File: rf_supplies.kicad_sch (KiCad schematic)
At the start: 27 parts, among them J20 VSENSE, U14 INA290A2xDCK

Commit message: wip
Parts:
- removed R100, R102, R104, R106: 453k, Resistor_SMD:R_0402_1005Metric, symbol Device:R_Small
- removed R101, R103, R105, R107: 33k, Resistor_SMD:R_0402_1005Metric, symbol Device:R_Small
- R109: value 60k -> 70k
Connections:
- no-connect marks 6 -> 2
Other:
- sheet Switching TX 6V renamed RF Switching 7V
- removed sheet Linear POL LMK DIG
- removed sheet Linear POL LMK VCO
- removed sheet Linear POL LMX
- removed sheet Linear POL LMX BUF
- removed sheet OP Amp Supply
- moved on the sheet: R108, R109

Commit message: Add Clock sources and monitor output
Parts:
- renumbered C102 to C106, C103 to C107, C104 to C108, C105 to C109, D11 to D10, J20 to J26, L6 to L5, R93 to R86, R94 to R87, R95 to R88, R96 to R89, R97 to R90, R98 to R91, R99 to R92, R108 to R93, R109 to R94, U14 to U20

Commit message: It's finished (well the draft)
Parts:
- added R?: 49.9k, Resistor_SMD:R_0402_1005Metric, symbol Device:R_Small
- added R?: 267k, Resistor_SMD:R_0402_1005Metric, symbol Device:R_Small
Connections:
- net +7V: now also R?.1
- net GND: now also R?.2
- net RF_ISENSE renamed RF12_ISENSE
- net RF_SENSE renamed RF12_SENSE
- new net RF7_SENSE: R?.1, R?.2
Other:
- moved on the sheet: R87, R88, R89, R90, R91, R92

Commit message: Round 1 review comments
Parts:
- added R?: 1.8k, Resistor_THT:R_Array_SIP4, symbol Device:R_Small
- added R?: 4.7k, Resistor_THT:R_Array_SIP4, symbol Device:R_Small
- R146: renamed from R93; value 357k -> 619k
- R147: renamed from R94; value 70k -> 49.9k
- gave numbers to parts that had none: 2
- renumbered C106 to C140, C107 to C141, C108 to C142, C109 to C143, J26 to J29, R86 to R137, R87 to R138, R88 to R139, R89 to R140, R90 to R141, R91 to R144, R92 to R145, U20 to U21
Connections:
- net +7V: now also R?.1
- net GND: now also R?.2
- new net RF Switching 7V/OUTS: R?.1, R?.2
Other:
- sheet RF Switching 7V ports: added OUTS; removed none
- sheet RF Switching PSU ports: added OUTS; removed none

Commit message: Round 2 Review, power tree cleanup
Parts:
- added FB?: 74279228600, Inductor_SMD:L_0603_1608Metric, symbol Device:FerriteBead_Small
- R156: renamed from R146; now not fitted
- R157: renamed from R147; now not fitted
- R158, R159: renamed from R?; now not fitted
- renumbered C140 to C142, C141 to C143, C142 to C144, C143 to C145, J29 to J30, R137 to R147, R138 to R148, R139 to R149, R140 to R150, R141 to R151, R142 to R152, R143 to R153, R144 to R154, R145 to R155
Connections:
- net +12V_RF: now also FB?.1
- net +7V: now also FB?.2
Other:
- note added: "1.1RPI"
- note added: "12VRF"
- note added: "3.3LMKDIG"
- note added: "3.3LMKVCO"
- note added: "3.3LMX"
- note added: "3.3LMXBUF"
- note added: "3.3MCU"
- note added: "3.3VAMP1"
- note added: "3.3VAMP2"
- note added: "3.3VLNA"
- note added: "3.3VRXDIG"
- note added: "3.3VTXDIG"
- note added: "4V"
- note added: "4VRX"
- note added: "5A FUSE + FILTER 250mV/A ISENSE"
- note added: "5V"
- note added: "7VLO"
- note added: "LMR36510ADDA 12V->5.0V1A"
- note added: "LT3042 4V->3.3V0.2A"
- note added: "LT3045 4V->3.3V0.5A"
- note added: "LT3045 7V/12V->5V0.5A"
- note added: "LT8625S uMOD 12V->4V8A"
- note added: "LT8625S uMOD 12V->7V8A"
- note added: "Regulator is for if we run into thermal issues"
- note added: "TLV73311PDBV 3.3V->1.1V0.3A"
- note added: "TLV73333PDBV 4V->3.3V0.3A"
- note added: "TLV73333PDBV 5V->3.3V0.3A"
- note added: "VBUS"
- note added: "VDC"
- note added: "x2"
- moved on the sheet: C142, C143, C144, C145, D10, F1, FB1, J30, L5, R147, R148, R149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

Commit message: Darrel Suggestions
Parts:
- R158, R159: footprint Resistor_THT:R_Array_SIP4 -> (none)
- gave numbers to parts that had none: 1
- renumbered FB1 to FB3, L5 to L3
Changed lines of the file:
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@@
 		(dnp no)
 		(fields_autoplaced yes)
-		(property "Reference" "#PWR0171"
+		(property "Reference" "#PWR0173"
 			(at 71.12 27.94 0)
 			(hide yes)
@@
 			(project "huskypointofload"
 				(path "/eb9c972b-d134-41da-be97-ece3f463f7e0/28dccbc8-62a2-4750-b12f-4e220cef19bd"
-					(reference "#PWR0171")
+					(reference "#PWR0173")
 					(unit 1)
 				)
@@
 		(dnp no)
 		(fields_autoplaced yes)
-		(property "Reference" "#PWR0189"
+		(property "Reference" "#PWR0193"
 			(at 394.97 36.83 0)
 			(hide yes)
@@
 			(project "huskypointofload"
 				(path "/eb9c972b-d134-41da-be97-ece3f463f7e0/28dccbc8-62a2-4750-b12f-4e220cef19bd"
-					(reference "#PWR0189")
+					(reference "#PWR0193")
 					(unit 1)
 				)
@@
 		(in_pos_files yes)
 		(dnp no)
-		(property "Reference" "#PWR0188"
+		(property "Reference" "#PWR0191"
 			(at 374.65 57.15 0)
 			(hide yes)
@@
 			(project "huskypointofload"
 				(path "/eb9c972b-d134-41da-be97-ece3f463f7e0/28dccbc8-62a2-4750-b12f-4e220cef19bd"
-					(reference "#PWR0188")
+					(reference "#PWR0191")
 					(unit 1)
 				)
@@
 		(dnp no)
 		(fields_autoplaced yes)
-		(property "Reference" "#PWR0184"
+		(property "Reference" "#PWR0186"
 			(at 311.15 29.21 0)
 			(hide yes)
@@
 			(project "huskypointofload"
 				(path "/eb9c972b-d134-41da-be97-ece3f463f7e0/28dccbc8-62a2-4750-b12f-4e220cef19bd"
-					(reference "#PWR0184")
+					(reference "#PWR0186")
 					(unit 1)
 				)
@@
 		(dnp no)
 		(fields_autoplaced yes)
-		(property "Reference" "#PWR0330"
+		(property "Reference" "#PWR0189"
 			(at 339.09 77.47 0)
 			(hide yes)
@@
 			(project "huskypointofload"
 				(path "/eb9c972b-d134-41da-be97-ece3f463f7e0/28dccbc8-62a2-4750-b12f-4e220cef19bd"
-					(reference "#PWR0330")
+					(reference "#PWR0189")
 					(unit 1)
 				)
@@
 		(in_pos_files yes)
 		(dnp no)
-		(property "Reference" "L5"
+		(property "Reference" "L3"
 			(at 139.7 23.622 90)
 			(show_name no)
@@
 			(project "huskypointofload"
 				(path "/eb9c972b-d134-41da-be97-ece3f463f7e0/28dccbc8-62a2-4750-b12f-4e220cef19bd"
-					(reference "L5")
+					(reference "L3")
 					(unit 1)
 				)
@@
 		(dnp no)
 		(fields_autoplaced yes)
-		(property "Reference" "#PWR0186"
+		(property "Reference" "#PWR0188"
 			(at 339.09 29.21 0)
 			(hide yes)
@@
 			(project "huskypointofload"
 				(path "/eb9c972b-d134-41da-be97-ece3f463f7e0/28dccbc8-62a2-4750-b12f-4e220cef19bd"
-					(reference "#PWR0186")
+					(reference "#PWR0188")
 					(unit 1)
 				)
@@
 		(in_pos_files yes)
 		(dnp no)
-		(property "Reference" "#PWR0187"
+		(property "Reference" "#PWR0190"
 			(at 374.65 29.21 0)
 			(hide yes)
@@
 			(project "huskypointofload"
 				(path "/eb9c972b-d134-41da-be97-ece3f463f7e0/28dccbc8-62a2-4750-b12f-4e220cef19bd"
-					(reference "#PWR0187")
+					(reference "#PWR0190")
 					(unit 1)
 				)
@@
 		(dnp no)
 		(fields_autoplaced yes)
-		(property "Reference" "#PWR0174"
+		(property "Reference" "#PWR0176"
 			(at 129.54 44.45 0)
 			(hide yes)
@@
 			(project "huskypointofload"
 				(path "/eb9c972b-d134-41da-be97-ece3f463f7e0/28dccbc8-62a2-4750-b12f-4e220cef19bd"
-					(reference "#PWR0174")
+					(reference "#PWR0176")
 					(unit 1)
 				)
@@
 		(in_pos_files yes)
 		(dnp no)
-		(property "Reference" "#PWR0331"
+		(property "Reference" "#PWR0192"
 			(at 374.65 77.47 0)
 			(hide yes)
@@
 			(project "huskypointofload"
 				(path "/eb9c972b-d134-41da-be97-ece3f463f7e0/28dccbc8-62a2-4750-b12f-4e220cef19bd"
-					(reference "#PWR0331")
+					(reference "#PWR0192")
 					(unit 1)
 				)
@@
 		(dnp no)
 		(fields_autoplaced yes)
-		(property "Reference" "#PWR0180"
+		(property "Reference" "#PWR0182"
 			(at 223.52 54.61 0)
 			(hide yes)
@@
 			(project "huskypointofload"
 				(path "/eb9c972b-d134-41da-be97-ece3f463f7e0/28dccbc8-62a2-4750-b12f-4e220cef19bd"
-					(reference "#PWR0180")
+					(reference "#PWR0182")
 					(unit 1)
 				)
@@
 		(dnp no)
 		(fields_autoplaced yes)
-		(property "Reference" "#PWR0182"
+		(property "Reference" "#PWR0184"
 			(at 247.65 54.61 0)
 			(hide yes)
@@
 			(project "huskypointofload"
 				(path "/eb9c972b-d134-41da-be97-ece3f463f7e0/28dccbc8-62a2-4750-b12f-4e220cef19bd"
-					(reference "#PWR0182")
+					(reference "#PWR0184")
 					(unit 1)
 				)
@@
 		(in_pos_files yes)
 		(dnp no)
-		(property "Reference" "#PWR0169"
+		(property "Reference" "#PWR0171"
 			(at 63.5 29.21 0)
 			(hide yes)
@@
 			(project "huskypointofload"
 				(path "/eb9c972b-d134-41da-be97-ece3f463f7e0/28dccbc8-62a2-4750-b12f-4e220cef19bd"
-					(reference "#PWR0169")
+					(reference "#PWR0171")
 					(unit 1)
 				)
@@
 		(dnp no)
 		(fields_autoplaced yes)
-		(property "Reference" "#PWR0176"
+		(property "Reference" "#PWR0180"
 			(at 199.39 54.61 0)
 			(hide yes)
@@
 			(project "huskypointofload"
 				(path "/eb9c972b-d134-41da-be97-ece3f463f7e0/28dccbc8-62a2-4750-b12f-4e220cef19bd"
-					(reference "#PWR0176")
+					(reference "#PWR0180")
 					(unit 1)
 				)
@@
 		(in_pos_files yes)
 		(dnp no)
-		(property "Reference" "#PWR0185"
+		(property "Reference" "#PWR0187"
 			(at 311.15 57.15 0)
 			(hide yes)
@@
 			(project "huskypointofload"
 				(path "/eb9c972b-d134-41da-be97-ece3f463f7e0/28dccbc8-62a2-4750-b12f-4e220cef19bd"
-					(reference "#PWR0185")
+					(reference "#PWR0187")
 					(unit 1)
 				)
@@
 		(dnp no)
 		(fields_autoplaced yes)
-		(property "Reference" "#PWR0175"
+		(property "Reference" "#PWR0179"
 			(at 199.39 29.21 0)
 			(hide yes)
@@
 			(project "huskypointofload"
 				(path "/eb9c972b-d134-41da-be97-ece3f463f7e0/28dccbc8-62a2-4750-b12f-4e220cef19bd"
-					(reference "#PWR0175")
+					(reference "#PWR0179")
 					(unit 1)
 				)
@@
 		(dnp no)
 		(fields_autoplaced yes)
-		(property "Reference" "#PWR0183"
+		(property "Reference" "#PWR0185"
 			(at 275.59 29.21 0)
 			(hide yes)
@@
 			(project "huskypointofload"
 				(path "/eb9c972b-d134-41da-be97-ece3f463f7e0/28dccbc8-62a2-4750-b12f-4e220cef19bd"
-					(reference "#PWR0183")
+					(reference "#PWR0185")
 					(unit 1)
 				)
@@
 		(dnp no)
 		(fields_autoplaced yes)
-		(property "Reference" "#PWR0179"
+		(property "Reference" "#PWR0181"
 			(at 223.52 29.21 0)
 			(hide yes)
@@
 			(project "huskypointofload"
 				(path "/eb9c972b-d134-41da-be97-ece3f463f7e0/28dccbc8-62a2-4750-b12f-4e220cef19bd"
-					(reference "#PWR0179")
+					(reference "#PWR0181")
 					(unit 1)
 				)
@@
 			)
 		)
-		(property "Footprint" "Resistor_THT:R_Array_SIP4"
+		(property "Footprint" ""
 			(at 379.73 27.94 0)
 			(hide yes)
@@
 		(dnp no)
 		(fields_autoplaced yes)
-		(property "Reference" "#PWR0172"
+		(property "Reference" "#PWR0174"
 			(at 100.33 44.45 0)
 			(hide yes)
@@
 			(project "huskypointofload"
 				(path "/eb9c972b-d134-41da-be97-ece3f463f7e0/28dccbc8-62a2-4750-b12f-4e220cef19bd"
-					(reference "#PWR0172")
+					(reference "#PWR0174")
 					(unit 1)
 				)
@@
 		(dnp no)
 		(fields_autoplaced yes)
-		(property "Reference" "#PWR0170"
+		(property "Reference" "#PWR0172"
 			(at 63.5 54.61 0)
 			(hide yes)
@@
 			(project "huskypointofload"
 				(path "/eb9c972b-d134-41da-be97-ece3f463f7e0/28dccbc8-62a2-4750-b12f-4e220cef19bd"
-					(reference "#PWR0170")
+					(reference "#PWR0172")
 					(unit 1)
 				)
@@
 		(in_pos_files yes)
 		(dnp no)
-		(property "Reference" "#PWR0181"
+		(property "Reference" "#PWR0183"
 			(at 247.65 29.21 0)
 			(hide yes)
@@
 			(project "huskypointofload"
 				(path "/eb9c972b-d134-41da-be97-ece3f463f7e0/28dccbc8-62a2-4750-b12f-4e220cef19bd"
-					(reference "#PWR0181")
+					(reference "#PWR0183")
 					(unit 1)
 				)
@@
 		(in_pos_files yes)
 		(dnp no)
-		(property "Reference" "FB?"
+		(property "Reference" "FB4"
 			(at 356.8319 69.85 90)
 			(show_name no)
@@
 			(project "huskypointofload"
 				(path "/eb9c972b-d134-41da-be97-ece3f463f7e0/28dccbc8-62a2-4750-b12f-4e220cef19bd"
-					(reference "FB?")
+					(reference "FB4")
 					(unit 1)
 				)
@@
 			)
 		)
-		(property "Footprint" "Resistor_THT:R_Array_SIP4"
+		(property "Footprint" ""
 			(at 389.89 27.94 0)
 			(hide yes)
@@
 		(dnp no)
 		(fields_autoplaced yes)
-		(property "Reference" "#PWR0173"
+		(property "Reference" "#PWR0175"
 			(at 114.3 44.45 0)
 			(hide yes)
@@
 			(project "huskypointofload"
 				(path "/eb9c972b-d134-41da-be97-ece3f463f7e0/28dccbc8-62a2-4750-b12f-4e220cef19bd"
-					(reference "#PWR0173")
+					(reference "#PWR0175")
 					(unit 1)
 				)
@@
 		(in_pos_files yes)
 		(dnp no)
-		(property "Reference" "FB1"
+		(property "Reference" "FB3"
 			(at 124.4219 21.59 90)
 			(show_name no)
@@
 			(project "huskypointofload"
 				(path "/eb9c972b-d134-41da-be97-ece3f463f7e0/28dccbc8-62a2-4750-b12f-4e220cef19bd"
-					(reference "FB1")
+					(reference "FB3")
 					(unit 1)
 				)

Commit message: Passive footprint pass
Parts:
- R158, R159: footprint (none) -> Resistor_SMD:R_0402_1005Metric
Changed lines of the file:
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@@
 			)
 		)
-		(property "Footprint" ""
+		(property "Footprint" "Resistor_SMD:R_0402_1005Metric"
 			(at 379.73 27.94 0)
 			(hide yes)
@@
 			)
 		)
-		(property "Footprint" ""
+		(property "Footprint" "Resistor_SMD:R_0402_1005Metric"
 			(at 389.89 27.94 0)
 			(hide yes)

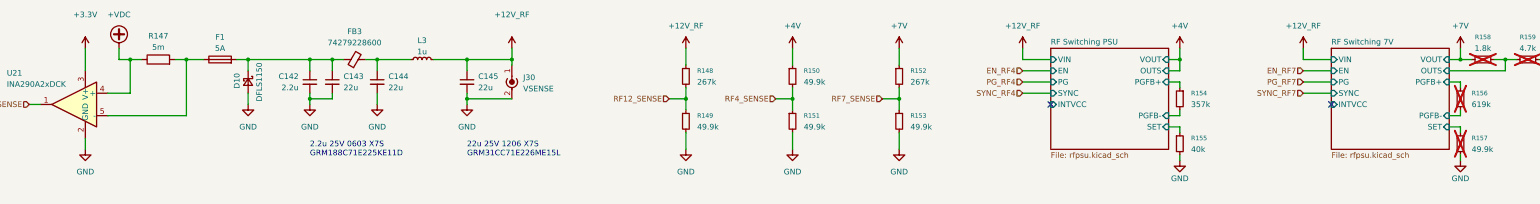
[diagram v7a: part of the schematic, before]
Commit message: add NC and fix ERC
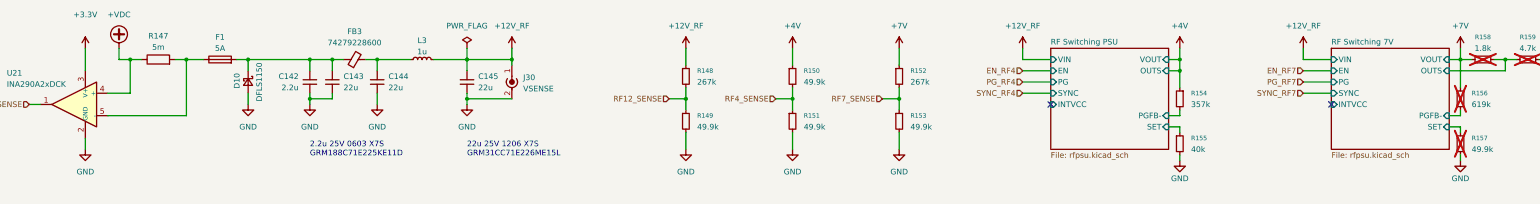
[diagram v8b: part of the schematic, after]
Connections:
- net RF Switching 7V/PGFB+ is gone; now on net +7V: R156.1
- net RF Switching PSU/PGFB+ is gone; now on net +4V: R154.1
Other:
- sheet RF Switching 7V ports: added none; removed PGFB+
- sheet RF Switching PSU ports: added none; removed PGFB+
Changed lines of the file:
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@@
 	)
 	(junction
+		(at 311.15 30.48)
+		(diameter 0)
+		(color 0 0 0 0)
+	)
+	(junction
 		(at 374.65 27.94)
 		(diameter 0)
@@
 	(wire
 		(pts
-			(xy 308.61 33.02) (xy 311.15 33.02)
-		)
-		(stroke
-			(width 0)
-			(type default)
-		)
-	)
-	(wire
-		(pts
 			(xy 384.81 27.94) (xy 387.35 27.94)
 		)
@@
 		)
 	)
-	(wire
-		(pts
-			(xy 374.65 34.29) (xy 374.65 33.02)
-		)
-		(stroke
-			(width 0)
-			(type default)
-		)
-	)
 	(polyline
 		(pts
@@
 		)
 	)
+	(wire
+		(pts
+			(xy 149.86 25.4) (xy 149.86 27.94)
+		)
+		(stroke
+			(width 0)
+			(type default)
+		)
+	)
+	(wire
+		(pts
+			(xy 311.15 30.48) (xy 311.15 34.29)
+		)
+		(stroke
+			(width 0)
+			(type default)
+		)
+	)
 	(polyline
 		(pts
@@
 	(wire
 		(pts
-			(xy 372.11 33.02) (xy 374.65 33.02)
-		)
-		(stroke
-			(width 0)
-			(type default)
-		)
-	)
-	(wire
-		(pts
 			(xy 100.33 27.94) (xy 97.79 27.94)
 		)
@@
 		)
 	)
-	(wire
-		(pts
-			(xy 311.15 34.29) (xy 311.15 33.02)
-		)
-		(stroke
-			(width 0)
-			(type default)
-		)
-	)
 	(polyline
 		(pts
@@
 	(wire
 		(pts
+			(xy 374.65 27.94) (xy 374.65 34.29)
+		)
+		(stroke
+			(width 0)
+			(type default)
+		)
+	)
+	(wire
+		(pts
 			(xy 308.61 27.94) (xy 311.15 27.94)
 		)
@@
 		)
 		(property "Value" "+12V_RF"
-			(at 160.02 17.78 0)
+			(at 160.02 20.32 0)
 			(show_name no)
 			(do_not_autoplace no)
@@
 		)
 	)
+	(symbol
+		(lib_id "power:PWR_FLAG")
+		(at 149.86 25.4 0)
+		(unit 1)
+		(body_style 1)
+		(exclude_from_sim no)
+		(in_bom yes)
+		(on_board yes)
+		(in_pos_files yes)
+		(dnp no)
+		(fields_autoplaced yes)
+		(property "Reference" "#FLG013"
+			(at 149.86 23.495 0)
+			(hide yes)
+			(show_name no)
+			(do_not_autoplace no)
+			(effects
+				(font
+					(size 1.27 1.27)
+				)
+			)
+		)
+		(property "Value" "PWR_FLAG"
+			(at 149.86 20.32 0)
+			(show_name no)
+			(do_not_autoplace no)
+			(effects
+				(font
+					(size 1.27 1.27)
+				)
+			)
+		)
+		(property "Footprint" ""
+			(at 149.86 25.4 0)
+			(hide yes)
+			(show_name no)
+			(do_not_autoplace no)
+			(effects
+				(font
+					(size 1.27 1.27)
+				)
+			)
+		)
+		(property "Datasheet" ""
+			(at 149.86 25.4 0)
+			(hide yes)
+			(show_name no)
+			(do_not_autoplace no)
+			(effects
+				(font
+					(size 1.27 1.27)
+				)
+			)
+		)
+		(property "Description" "Special symbol for telling ERC where power comes from"
+			(at 149.86 25.4 0)
+			(hide yes)
+			(show_name no)
+			(do_not_autoplace no)
+			(effects
+				(font
+					(size 1.27 1.27)
+				)
+			)
+		)
+		(pin "1"
+		)
+		(instances
+			(project "huskypointofload"
+				(path "/eb9c972b-d134-41da-be97-ece3f463f7e0/28dccbc8-62a2-4750-b12f-4e220cef19bd"
+					(reference "#FLG013")
+					(unit 1)
+				)
+			)
+		)
+	)
 	(sheet
 		(at 345.44 25.4)
@@
 			)
 		)
-		(pin "PGFB+" input
-			(at 372.11 33.02 0)
-			(effects
-				(font
-					(size 1.27 1.27)
-				)
-				(justify right)
-			)
-		)
 		(pin "PGFB-" input
 			(at 372.11 40.64 0)
@@
 			)
 		)
-		(pin "PGFB+" input
-			(at 308.61 33.02 0)
-			(effects
-				(font
-					(size 1.27 1.27)
-				)
-				(justify right)
-			)
-		)
